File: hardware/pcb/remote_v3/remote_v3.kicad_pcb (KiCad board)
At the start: 2 copper layers, 109.2 x 71.1 mm, 32 parts

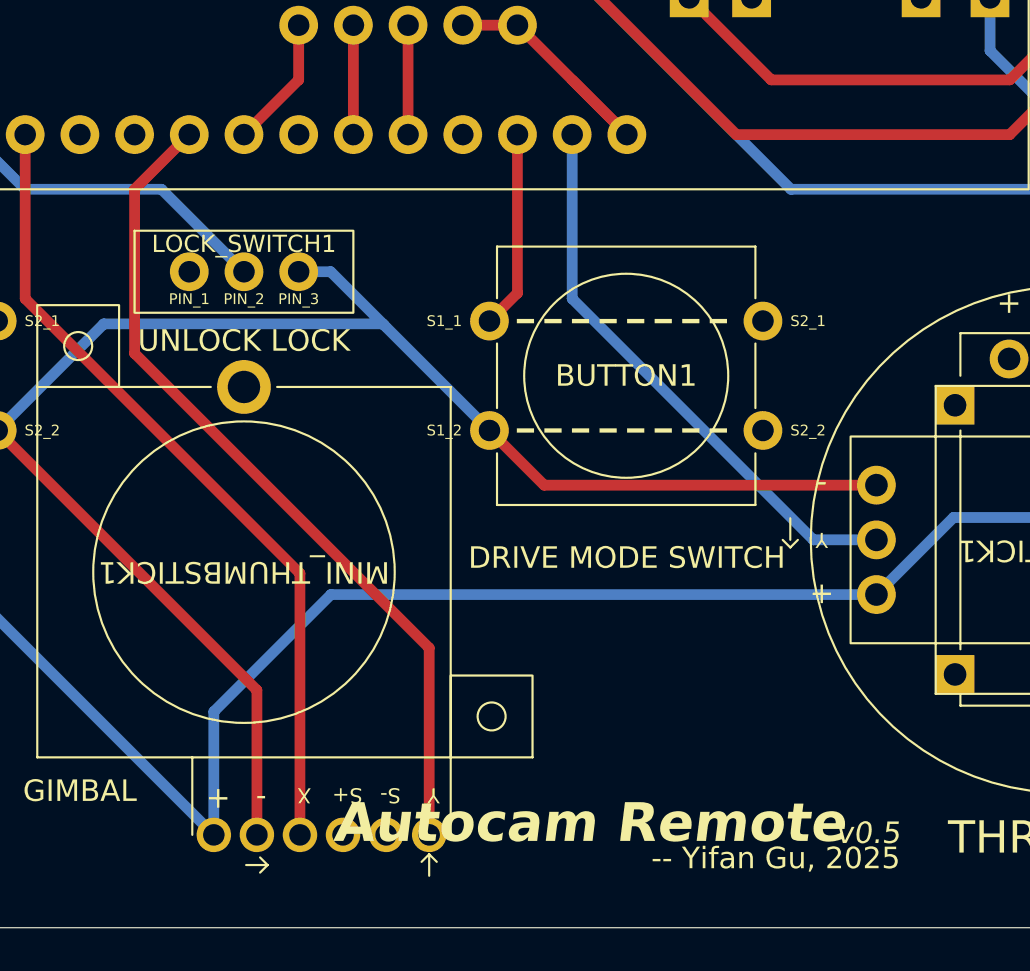
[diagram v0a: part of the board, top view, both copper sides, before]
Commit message: remote: Update PCB for remote.
Fix the issue that GPIO 35 does not have internal PULLUP resistor.
So switch the pin with the gimbal thumbstick input Y, instead of the
drive mode button.

Update sensor and tag pcb as well to reflect the changes.
- tag: Use pin 39 for battery measurement and revert the resistor value
  change that's done in the previous commit.
- sensor: Fix a wiring issue.
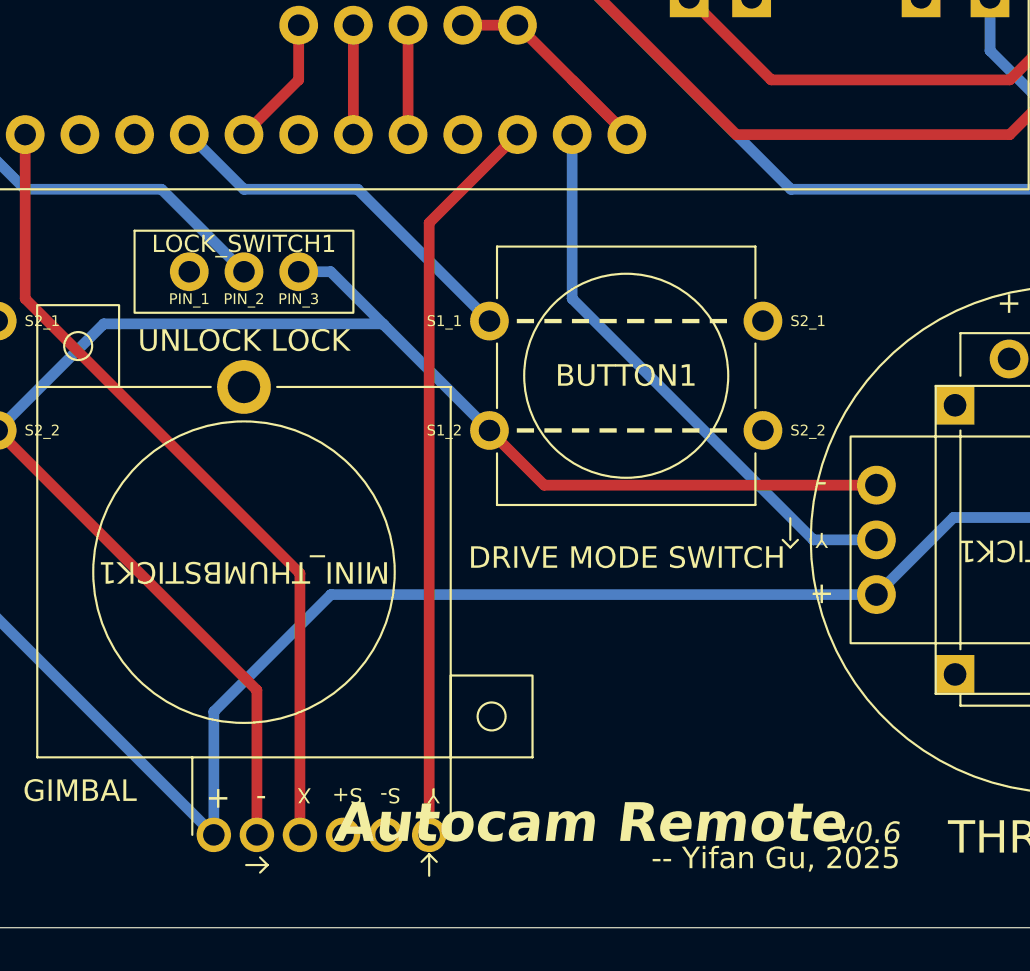
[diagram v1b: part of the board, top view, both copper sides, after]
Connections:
- ESP32_UWB1 pad 12: Net-(ESP32_UWB1-IO25) -> Net-(BUTTON1-S1_1)
- ESP32_UWB1 pad 18: Net-(BUTTON1-S1_1) -> Net-(ESP32_UWB1-IO35)
- MINI_THUMBSTICK1 pad 6: Net-(ESP32_UWB1-IO25) -> Net-(ESP32_UWB1-IO35)
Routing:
- net Net-(ESP32_UWB1-IO25): track 39.7 -> 0.00 mm
- net Net-(ESP32_UWB1-IO35): track 0.00 -> 34.2 mm
- net Net-(BUTTON1-S1_1): track 9.20 -> 18.0 mm
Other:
- board text added: "v0.6"
- board text removed: "v0.5"
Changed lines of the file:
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@@
 	(title_block
 		(title "Autocam Remote")
-		(date "2025-03-18")
-		(rev "v0.5")
+		(date "2025-03-27")
+		(rev "v0.6")
 	)
 	(layers
@@
 	(net 5 "unconnected-(3.7V_BATTERY_CHARGER1-B--Pad5)")
 	(net 6 "Net-(3.7V_BATTERY_CHARGER1-OUT-)")
-	(net 7 "Net-(ESP32_UWB1-IO25)")
+	(net 7 "Net-(ESP32_UWB1-IO35)")
 	(net 8 "unconnected-(BUTTON2-S1_2-Pad2)")
 	(net 9 "Net-(ESP32_UWB1-3V3)")
@@
 		)
 		(sheetname "/")
-		(sheetfile "remote_v2.kicad_sch")
+		(sheetfile "remote_v3.kicad_sch")
 		(fp_circle
 			(center 0 0)
@@
 		)
 		(sheetname "/")
-		(sheetfile "remote_v2.kicad_sch")
+		(sheetfile "remote_v3.kicad_sch")
 		(fp_line
 			(start 12.7 0)
@@
 		)
 		(sheetname "/")
-		(sheetfile "remote_v2.kicad_sch")
+		(sheetfile "remote_v3.kicad_sch")
 		(fp_rect
 			(start 0 0)
@@
 			(layers "*.Cu" "*.Mask")
 			(remove_unused_layers no)
-			(net 7 "Net-(ESP32_UWB1-IO25)")
+			(net 66 "Net-(BUTTON1-S1_1)")
 			(pinfunction "IO25")
 			(pintype "bidirectional")
@@
 			(layers "*.Cu" "*.Mask")
 			(remove_unused_layers no)
-			(net 66 "Net-(BUTTON1-S1_1)")
+			(net 7 "Net-(ESP32_UWB1-IO35)")
 			(pinfunction "IO35")
 			(pintype "bidirectional")
@@
 		)
 		(sheetname "/")
-		(sheetfile "remote_v2.kicad_sch")
+		(sheetfile "remote_v3.kicad_sch")
 		(fp_rect
 			(start -2.54 -1.905)
@@
 		)
 		(sheetname "/")
-		(sheetfile "remote_v2.kicad_sch")
+		(sheetfile "remote_v3.kicad_sch")
 		(fp_line
 			(start -6 -6)
@@
 		)
 		(sheetname "/")
-		(sheetfile "remote_v2.kicad_sch")
+		(sheetfile "remote_v3.kicad_sch")
 		(fp_circle
 			(center 0 0)
@@
 		)
 		(sheetname "/")
-		(sheetfile "remote_v2.kicad_sch")
+		(sheetfile "remote_v3.kicad_sch")
 		(fp_line
 			(start 12.7 0)
@@
 		)
 		(sheetname "/")
-		(sheetfile "remote_v2.kicad_sch")
+		(sheetfile "remote_v3.kicad_sch")
 		(fp_line
 			(start -6 -6)
@@
 		)
 		(sheetname "/")
-		(sheetfile "remote_v2.kicad_sch")
+		(sheetfile "remote_v3.kicad_sch")
 		(fp_line
 			(start 9.6 -8.6)
@@
 			(layers "*.Cu" "*.Mask")
 			(remove_unused_layers no)
-			(net 7 "Net-(ESP32_UWB1-IO25)")
+			(net 7 "Net-(ESP32_UWB1-IO35)")
 			(pinfunction "Y")
 			(pintype "output")
@@
 		)
 		(sheetname "/")
-		(sheetfile "remote_v2.kicad_sch")
+		(sheetfile "remote_v3.kicad_sch")
 		(fp_circle
 			(center 0 0)
@@
 		)
 		(sheetname "/")
-		(sheetfile "remote_v2.kicad_sch")
+		(sheetfile "remote_v3.kicad_sch")
 		(fp_circle
 			(center 0 0)
@@
 		)
 		(sheetname "/")
-		(sheetfile "remote_v2.kicad_sch")
+		(sheetfile "remote_v3.kicad_sch")
 		(fp_rect
 			(start -2.54 -1.905)
@@
 		)
 		(sheetname "/")
-		(sheetfile "remote_v2.kicad_sch")
+		(sheetfile "remote_v3.kicad_sch")
 		(fp_rect
 			(start -2.54 -1.905)
@@
 		)
 		(sheetname "/")
-		(sheetfile "remote_v2.kicad_sch")
+		(sheetfile "remote_v3.kicad_sch")
 		(fp_circle
 			(center 0 0)
@@
 		(property ki_fp_filters "R_*")
 		(sheetname "/")
-		(sheetfile "remote_v2.kicad_sch")
+		(sheetfile "remote_v3.kicad_sch")
 		(fp_rect
 			(start -1.27 1.27)
@@
 		(property ki_fp_filters "R_*")
 		(sheetname "/")
-		(sheetfile "remote_v2.kicad_sch")
+		(sheetfile "remote_v3.kicad_sch")
 		(fp_rect
 			(start -1.27 1.27)
@@
 		)
 		(sheetname "/")
-		(sheetfile "remote_v2.kicad_sch")
+		(sheetfile "remote_v3.kicad_sch")
 		(fp_rect
 			(start -5.9 5.8)
@@
 		(property ki_fp_filters "R_*")
 		(sheetname "/")
-		(sheetfile "remote_v2.kicad_sch")
+		(sheetfile "remote_v3.kicad_sch")
 		(fp_rect
 			(start -1.27 1.27)
@@
 		(property ki_fp_filters "R_*")
 		(sheetname "/")
-		(sheetfile "remote_v2.kicad_sch")
+		(sheetfile "remote_v3.kicad_sch")
 		(fp_rect
 			(start -1.27 1.27)
@@
 		(property ki_fp_filters "R_*")
 		(sheetname "/")
-		(sheetfile "remote_v2.kicad_sch")
+		(sheetfile "remote_v3.kicad_sch")
 		(fp_rect
 			(start -1.27 1.27)
@@
 		(property ki_fp_filters "R_*")
 		(sheetname "/")
-		(sheetfile "remote_v2.kicad_sch")
+		(sheetfile "remote_v3.kicad_sch")
 		(fp_rect
 			(start -1.27 1.27)
@@
 		(property ki_fp_filters "R_*")
 		(sheetname "/")
-		(sheetfile "remote_v2.kicad_sch")
+		(sheetfile "remote_v3.kicad_sch")
 		(fp_rect
 			(start -1.27 1.27)
@@
 		(property ki_fp_filters "R_*")
 		(sheetname "/")
-		(sheetfile "remote_v2.kicad_sch")
+		(sheetfile "remote_v3.kicad_sch")
 		(fp_rect
 			(start -1.27 1.27)
@@
 		)
 		(sheetname "/")
-		(sheetfile "remote_v2.kicad_sch")
+		(sheetfile "remote_v3.kicad_sch")
 		(fp_rect
 			(start 0 17.4)
@@
 		(property ki_fp_filters "R_*")
 		(sheetname "/")
-		(sheetfile "remote_v2.kicad_sch")
+		(sheetfile "remote_v3.kicad_sch")
 		(fp_rect
 			(start -1.27 1.27)
@@
 		(property ki_fp_filters "R_*")
 		(sheetname "/")
-		(sheetfile "remote_v2.kicad_sch")
+		(sheetfile "remote_v3.kicad_sch")
 		(fp_rect
 			(start -1.27 1.27)
@@
 		(layer "Edge.Cuts")
 	)
-	(gr_text "v0.5"
+	(gr_text "v0.6"
 		(at 177.8 134.62 0)
 		(layer "F.SilkS")
@@
 			(justify right bottom)
 		)
-		(render_cache "v0.5" 0
+		(render_cache "v0.6" 0
 			(polygon
 				(pts
@@
 			(polygon
 				(pts
-					(xy 177.705967 134.45) (xy 177.208322 134.45) (xy 177.311392 134.35621) (xy 177.620665 134.35621)
+					(xy 177.705967 134.45) (xy 177.208322 134.45) (xy 177.311453 134.35621) (xy 177.620726 134.35621)
+				)
+			)
+			(polygon
+				(pts
+					(xy 177.317804 134.082109) (xy 177.296188 134.33661) (xy 177.191774 134.43046) (xy 177.224869 134.059211)
+					(xy 177.263032 134.022391)
 				)
 			)
@@
 			(polygon
 				(pts
-					(xy 177.758173 134.059272) (xy 177.725079 134.43046) (xy 177.639777 134.33661) (xy 177.661453 134.082231)
+					(xy 177.758173 134.059272) (xy 177.725079 134.43217) (xy 177.639777 134.336671) (xy 177.661453 134.082231)
 					(xy 177.726361 134.022391)
 				)
@@
 				(pts
 					(xy 177.666521 133.957606) (xy 177.711096 134.004501) (xy 177.657606 134.051395) (xy 177.325436 134.051395)
-					(xy 177.283426 134.004501) (xy 177.334351 133.957606)
+					(xy 177.283426 134.004562) (xy 177.334351 133.957789)
 				)
 			)
@@
 	)
 	(segment
-		(start 144.78 101.6)
-		(end 142.24 104.14)
-		(width 0.5)
-		(layer "F.Cu")
-		(net 7)
-	)
-	(segment
-		(start 155.92 125.44)
-		(end 155.92 134.12)
-		(width 0.5)
-		(layer "F.Cu")
-		(net 7)
-	)
-	(segment
-		(start 142.24 111.76)
-		(end 155.92 125.44)
+		(start 155.92 105.7)
+		(end 160.02 101.6)
 		(width 0.5)
 		(layer "F.Cu")
@@
 	)
 	(segment
-		(start 142.24 104.14)
-		(end 142.24 111.76)
+		(start 155.92 134.12)
+		(end 155.92 105.7)
 		(width 0.5)
 		(layer "F.Cu")
@@
 	)
 	(segment
-		(start 144.78 101.6)
-		(end 145.260182 101.6)
-		(width 0.3)
-		(layer "B.Cu")
-		(net 7)
-	)
-	(segment
 		(start 99.06 80.01)
 		(end 106.68 80.01)
@@
 	)
 	(segment
-		(start 160.02 108.960058)
-		(end 160.02 101.6)
+		(start 147.32 104.14)
+		(end 144.78 101.6)
 		(width 0.5)
-		(layer "F.Cu")
+		(layer "B.Cu")
+		(net 66)
+	)
+	(segment
+		(start 152.599942 104.14)
+		(end 147.32 104.14)
+		(width 0.5)
+		(layer "B.Cu")
 		(net 66)
 	)
 	(segment
 		(start 158.72 110.260058)
-		(end 160.02 108.960058)
+		(end 152.599942 104.14)
 		(width 0.5)
-		(layer "F.Cu")
+		(layer "B.Cu")
+		(net 66)
+	)
+	(segment
+		(start 144.78 101.6)
+		(end 145.260182 101.6)
+		(width 0.3)
+		(layer "B.Cu")
 		(net 66)
 	)
